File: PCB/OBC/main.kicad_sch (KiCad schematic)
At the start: 33 parts, among them J7 USB_C_Receptacle_USB2.0_16P, U2 STM32F405RGTx, U5 USBLC6-2SC6

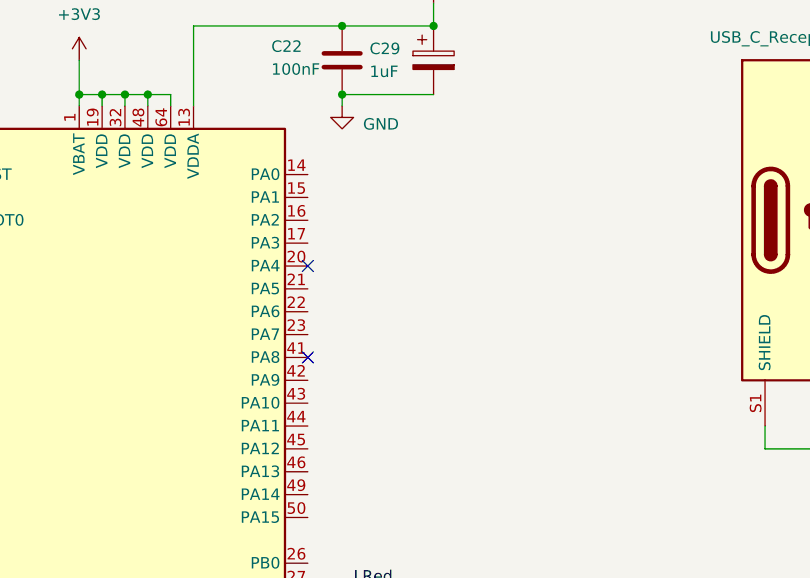
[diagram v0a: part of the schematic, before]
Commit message: Add: flash memory and mux at libraries
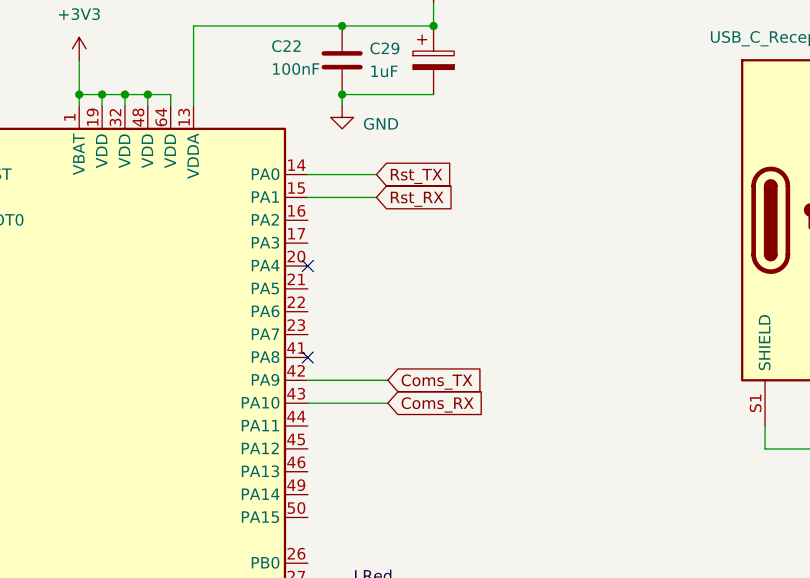
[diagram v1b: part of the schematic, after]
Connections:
- net Rst_TX: now reaches U2.14 (PA0)
- net Rst_RX: now reaches U2.15 (PA1)
- net Coms_TX: now reaches U2.42 (PA9)
- net Coms_RX: now reaches U2.43 (PA10)
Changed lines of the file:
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@@
+	(wire
+		(pts
+			(xy 156.21 67.31) (xy 165.1 67.31)
+		)
+		(stroke
+			(width 0)
+			(type default)
+		)
+	)
 	(wire
 		(pts
@@
 	(wire
 		(pts
+			(xy 156.21 46.99) (xy 163.83 46.99)
+		)
+		(stroke
+			(width 0)
+			(type default)
+		)
+	)
+	(wire
+		(pts
 			(xy 130.81 35.56) (xy 130.81 36.83)
 		)
@@
 	(wire
 		(pts
+			(xy 156.21 69.85) (xy 165.1 69.85)
+		)
+		(stroke
+			(width 0)
+			(type default)
+		)
+	)
+	(wire
+		(pts
 			(xy 73.66 26.67) (xy 62.23 26.67)
 		)
@@
 		(pts
 			(xy 233.68 41.91) (xy 229.87 41.91)
+		)
+		(stroke
+			(width 0)
+			(type default)
+		)
+	)
+	(wire
+		(pts
+			(xy 156.21 44.45) (xy 163.83 44.45)
 		)
 		(stroke
@@
 			)
 			(justify right bottom)
+		)
+	)
+	(global_label "Rst_RX"
+		(shape input)
+		(at 163.83 46.99 0)
+		(fields_autoplaced yes)
+		(effects
+			(font
+				(size 1.27 1.27)
+			)
+			(justify left)
+		)
+		(property "Intersheetrefs" "${INTERSHEET_REFS}"
+			(at 173.2861 46.99 0)
+			(effects
+				(font
+					(size 1.27 1.27)
+				)
+				(justify left)
+				(hide yes)
+			)
 		)
 	)
@@
 		)
 	)
+	(global_label "Coms_RX"
+		(shape input)
+		(at 165.1 69.85 0)
+		(fields_autoplaced yes)
+		(effects
+			(font
+				(size 1.27 1.27)
+			)
+			(justify left)
+		)
+		(property "Intersheetrefs" "${INTERSHEET_REFS}"
+			(at 176.6727 69.85 0)
+			(effects
+				(font
+					(size 1.27 1.27)
+				)
+				(justify left)
+				(hide yes)
+			)
+		)
+	)
 	(global_label "LDO_USB"
 		(shape input)
@@
 		)
 	)
+	(global_label "Coms_TX"
+		(shape input)
+		(at 165.1 67.31 0)
+		(fields_autoplaced yes)
+		(effects
+			(font
+				(size 1.27 1.27)
+			)
+			(justify left)
+		)
+		(property "Intersheetrefs" "${INTERSHEET_REFS}"
+			(at 176.3703 67.31 0)
+			(effects
+				(font
+					(size 1.27 1.27)
+				)
+				(justify left)
+				(hide yes)
+			)
+		)
+	)
 	(global_label "USB_D+"
 		(shape input)
@@
 			(effects
 				(font
+					(size 1.27 1.27)
+				)
+				(justify left)
+				(hide yes)
+			)
+		)
+	)
+	(global_label "Rst_TX"
+		(shape input)
+		(at 163.83 44.45 0)
+		(fields_autoplaced yes)
+		(effects
+			(font
+				(size 1.27 1.27)
+			)
+			(justify left)
+		)
+		(property "Intersheetrefs" "${INTERSHEET_REFS}"
+			(at 172.9837 44.45 0)
+			(effects
+				(font

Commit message: Watchdog
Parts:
- added C10, C11: 100nF, symbol Device:C
- added C12: 1uF, symbol Device:C
- added R3, R4: 10k, symbol Device:R
- added U3: W25Q128JVSIQ, SOIC_128JVSIQ_WIN, symbol W25Q128JVSIQ:W25Q128JVSIQ
- added U6: TMUX1574PWR, PWP16_2P31X2P46_TEX, symbol TMUX1574PWR:TMUX1574PWR
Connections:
- net +3V3: now also C10.1, C11.1, C12.1, R3.2, R4.1, U3.8 (VCC), U6.16 (VDD)
- net GND: now also C10.2, C11.2, C12.2, U3.1 (/CS), U3.4 (GND), U6.15 (*EN), U6.8 (GND)
- new net: R3.1, U3.3
- new net: R4.2, U3.7 (/HOLD_or_/RESET_(IO3))
- new net py_flash_clk_m: U3.6 (CLK), U6.12 (D4)
- new net py_flash_miso_m: U3.2 (DO_(IO1)), U6.7 (D2)
- new net py_flash_mosi_m: U3.5 (DI_(IO0)), U6.9 (D3)
- new net select_py: U6.1 (SEL)
- no-connect marks 9 -> 10
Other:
- moved on the sheet: C20, C21, C22, C29, C32, D3, D7, D8, J7, R14, R15, R16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

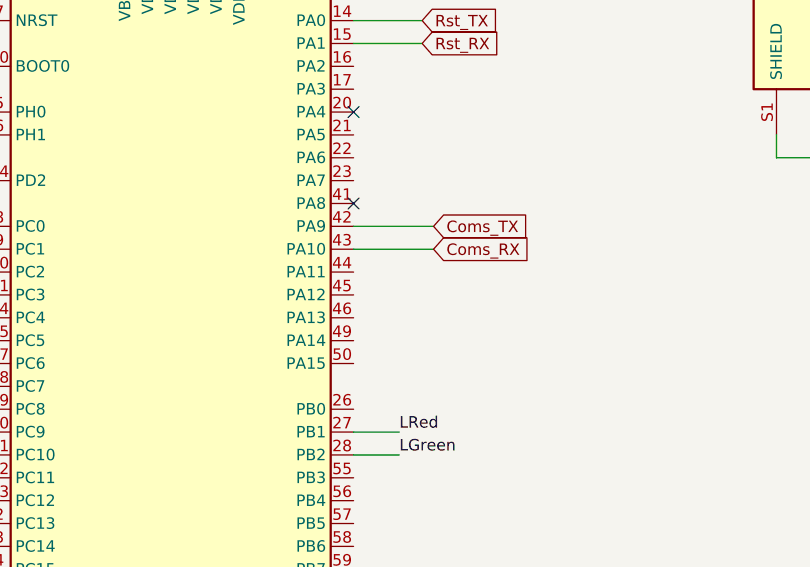
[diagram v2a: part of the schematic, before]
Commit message: Colocacion de OCP, LDO
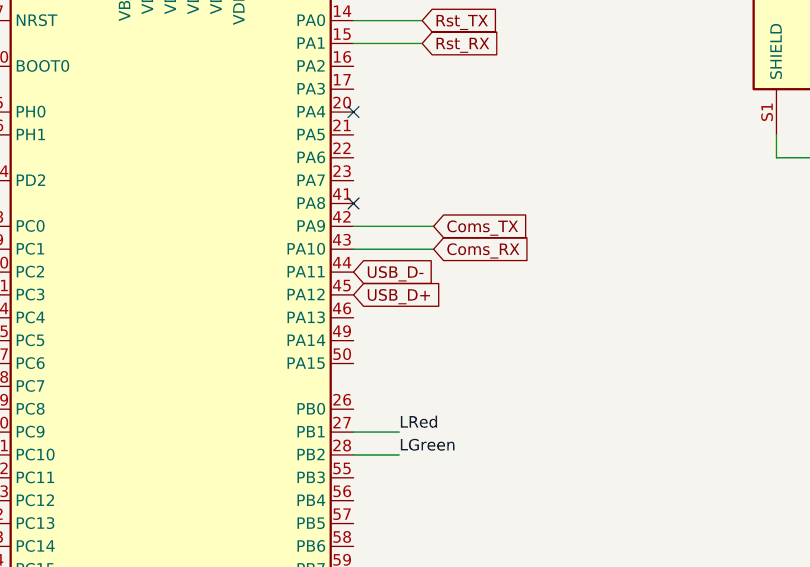
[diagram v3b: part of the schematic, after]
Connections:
- net USB_D+: now also U2.45 (PA12)
- net USB_D-: now also U2.44 (PA11)
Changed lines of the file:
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@@
+	(global_label "USB_D-"
+		(shape input)
+		(at 143.51 77.47 0)
+		(fields_autoplaced yes)
+		(effects
+			(font
+				(size 1.27 1.27)
+			)
+			(justify left)
+		)
+		(property "Intersheetrefs" "${INTERSHEET_REFS}"
+			(at 154.1152 77.47 0)
+			(effects
+				(font
+					(size 1.27 1.27)
+				)
+				(justify left)
+				(hide yes)
+			)
+		)
+	)
 	(global_label "USB_D-"
 		(shape input)
@@
 			(effects
 				(font
+					(size 1.27 1.27)
+				)
+				(justify left)
+				(hide yes)
+			)
+		)
+	)
+	(global_label "USB_D+"
+		(shape input)
+		(at 143.51 80.01 0)
+		(fields_autoplaced yes)
+		(effects
+			(font
+				(size 1.27 1.27)
+			)
+			(justify left)
+		)
+		(property "Intersheetrefs" "${INTERSHEET_REFS}"
+			(at 154.1152 80.01 0)
+			(effects
+				(font

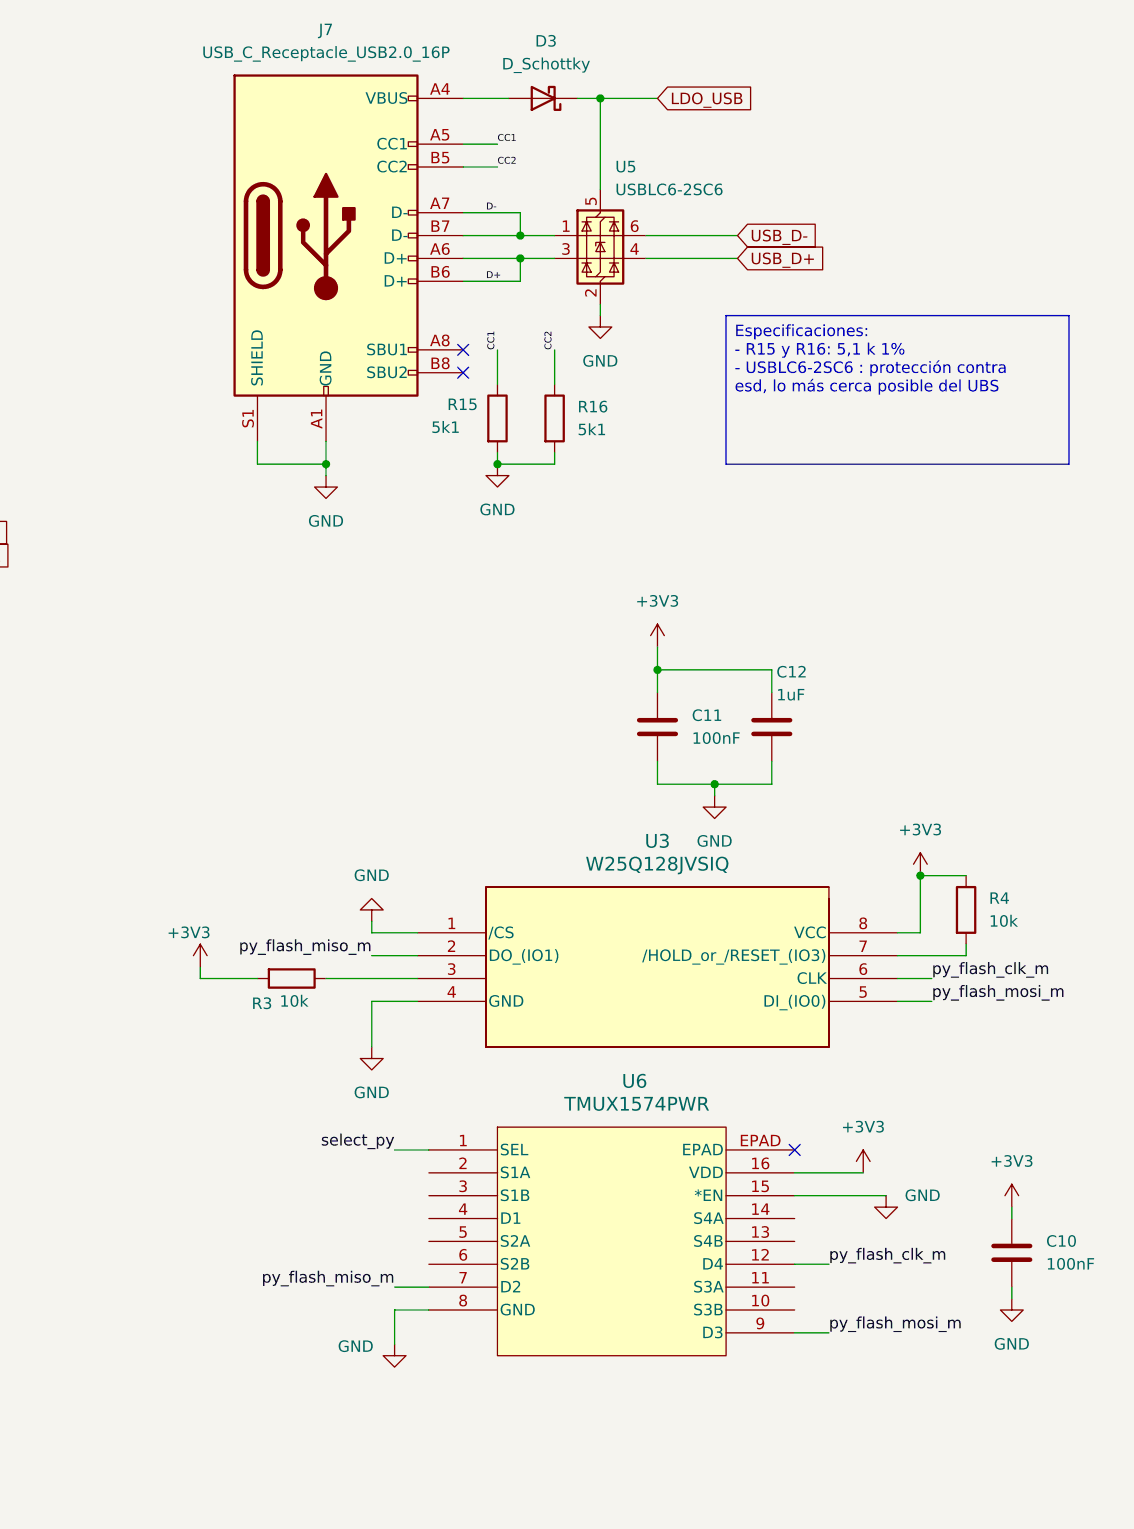
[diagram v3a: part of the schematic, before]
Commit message: Add: Can bus
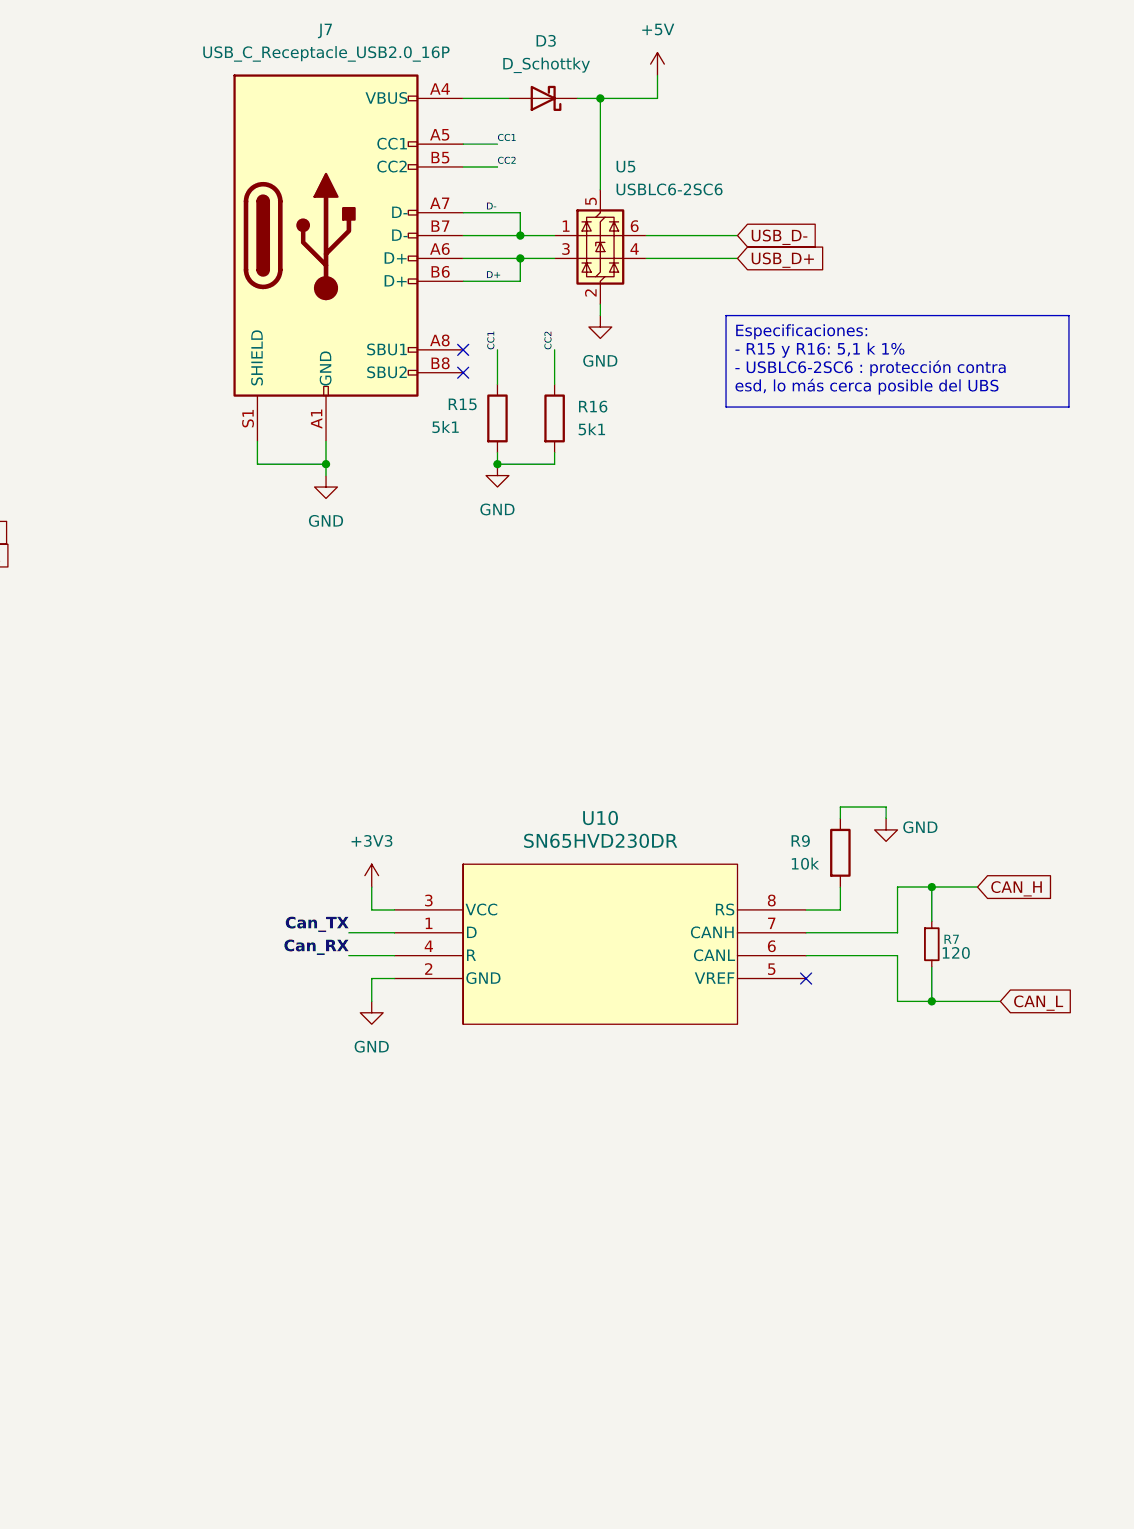
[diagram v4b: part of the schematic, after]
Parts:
- removed C10, C11: 100nF, symbol Device:C
- removed C12: 1uF, symbol Device:C
- removed R3, R4: 10k, symbol Device:R
- removed U3: W25Q128JVSIQ, SOIC_128JVSIQ_WIN, symbol W25Q128JVSIQ:W25Q128JVSIQ
- removed U6: TMUX1574PWR, PWP16_2P31X2P46_TEX, symbol TMUX1574PWR:TMUX1574PWR
- added R7: 120, symbol Device:R_Small
- added R9: 10k, symbol Device:R
- added U10: SN65HVD230DR, D8, symbol SN65HVD230DR:SN65HVD230DR
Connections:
- net +3V3: now also U10.3 (VCC)
- net GND: now also R9.1, U10.2 (GND)
- net LDO_USB renamed +5V
- new net: R9.2, U10.8 (RS)
- new net CAN_H: R7.1, U10.7 (CANH)
- new net CAN_L: R7.2, U10.6 (CANL)
- new net Can_RX: U10.4 (R)
- new net Can_TX: U10.1 (D)

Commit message: minors changes
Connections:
- net SWDIO1: now reaches U2.46 (PA13)
- net SWCLK1: now reaches U2.49 (PA14)
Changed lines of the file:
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@@
 	(wire
 		(pts
-			(xy 143.51 72.39) (xy 152.4 72.39)
+			(xy 143.51 72.39) (xy 151.13 72.39)
 		)
 		(stroke
@@
 	(wire
 		(pts
+			(xy 143.51 85.09) (xy 151.13 85.09)
+		)
+		(stroke
+			(width 0)
+			(type default)
+		)
+	)
+	(wire
+		(pts
+			(xy 151.13 80.01) (xy 143.51 80.01)
+		)
+		(stroke
+			(width 0)
+			(type default)
+		)
+	)
+	(wire
+		(pts
 			(xy 39.37 35.56) (xy 27.94 35.56)
 		)
@@
 	(wire
 		(pts
+			(xy 151.13 77.47) (xy 143.51 77.47)
+		)
+		(stroke
+			(width 0)
+			(type default)
+		)
+	)
+	(wire
+		(pts
 			(xy 63.5 46.99) (xy 63.5 49.53)
 		)
@@
 	(wire
 		(pts
+			(xy 143.51 82.55) (xy 151.13 82.55)
+		)
+		(stroke
+			(width 0)
+			(type default)
+		)
+	)
+	(wire
+		(pts
 			(xy 265.43 120.65) (xy 265.43 124.46)
 		)
@@
 	(wire
 		(pts
-			(xy 143.51 74.93) (xy 152.4 74.93)
+			(xy 143.51 74.93) (xy 151.13 74.93)
 		)
 		(stroke
@@
 	(global_label "USB_D-"
 		(shape input)
-		(at 143.51 77.47 0)
+		(at 151.13 77.47 0)
 		(fields_autoplaced yes)
 		(effects
@@
 		)
 		(property "Intersheetrefs" "${INTERSHEET_REFS}"
-			(at 154.1152 77.47 0)
+			(at 161.7352 77.47 0)
 			(effects
 				(font
@@
 	(global_label "Coms_RX"
 		(shape input)
-		(at 152.4 74.93 0)
+		(at 151.13 74.93 0)
 		(fields_autoplaced yes)
 		(effects
@@
 		)
 		(property "Intersheetrefs" "${INTERSHEET_REFS}"
-			(at 163.9727 74.93 0)
+			(at 162.7027 74.93 0)
+			(effects
+				(font
+					(size 1.27 1.27)
+				)
+				(justify left)
+				(hide yes)
+			)
+		)
+	)
+	(global_label "SWDIO1"
+		(shape input)
+		(at 151.13 82.55 0)
+		(fields_autoplaced yes)
+		(effects
+			(font
+				(size 1.27 1.27)
+			)
+			(justify left)
+		)
+		(property "Intersheetrefs" "${INTERSHEET_REFS}"
+			(at 161.1909 82.55 0)
+			(effects
+				(font
+					(size 1.27 1.27)
+				)
+				(justify left)
+				(hide yes)
+			)
+		)
+	)
+	(global_label "SWCLK1"
+		(shape input)
+		(at 151.13 85.09 0)
+		(fields_autoplaced yes)
+		(effects
+			(font
+				(size 1.27 1.27)
+			)
+			(justify left)
+		)
+		(property "Intersheetrefs" "${INTERSHEET_REFS}"
+			(at 161.5537 85.09 0)
 			(effects
 				(font
@@
 	(global_label "Coms_TX"
 		(shape input)
-		(at 152.4 72.39 0)
+		(at 151.13 72.39 0)
 		(fields_autoplaced yes)
 		(effects
@@
 		)
 		(property "Intersheetrefs" "${INTERSHEET_REFS}"
-			(at 163.6703 72.39 0)
+			(at 162.4003 72.39 0)
 			(effects
 				(font
@@
 	(global_label "USB_D+"
 		(shape input)
-		(at 143.51 80.01 0)
+		(at 151.13 80.01 0)
 		(fields_autoplaced yes)
 		(effects
@@
 		)
 		(property "Intersheetrefs" "${INTERSHEET_REFS}"
-			(at 154.1152 80.01 0)
+			(at 161.7352 80.01 0)
 			(effects
 				(font

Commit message: cambiode OCP
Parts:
- removed C20, C21: 2.2uF, Capacitor_SMD:C_0805_2012Metric_Pad1.18x1.45mm_HandSolder, symbol Device:C
- removed C24, C26: 100nF, Capacitor_SMD:C_0805_2012Metric_Pad1.18x1.45mm_HandSolder, symbol Device:C
- removed C25, C32: 100nF, Capacitor_SMD:C_0603_1608Metric_Pad1.08x0.95mm_HandSolder, symbol Device:C
- removed C28: 4.7u, Capacitor_SMD:C_0805_2012Metric_Pad1.18x1.45mm_HandSolder, symbol Device:C_Polarized
- removed C29: 1uF, Capacitor_SMD:C_0805_2012Metric_Pad1.18x1.45mm_HandSolder, symbol Device:C_Polarized
- removed C5: 15pF, Capacitor_SMD:C_0603_1608Metric_Pad1.08x0.95mm_HandSolder, symbol Device:C
- removed D8: LED, LED_SMD:LED_0805_2012Metric_Pad1.15x1.40mm_HandSolder, symbol Device:LED
- removed U2: STM32F405RGTx, Package_QFP:LQFP-64_10x10mm_P0.5mm, symbol MCU_ST_STM32F4:STM32F405RGTx
- added C1: 4.7u, Capacitor_SMD:C_0805_2012Metric_Pad1.18x1.45mm_HandSolder, symbol Device:C_Polarized
- added C10, C2: 15pF, Capacitor_SMD:C_0603_1608Metric_Pad1.08x0.95mm_HandSolder, symbol Device:C
- added C11: 100nF, Capacitor_SMD:C_0805_2012Metric_Pad1.18x1.45mm_HandSolder, symbol Device:C
- added C12, C15: 2.2uF, Capacitor_SMD:C_0805_2012Metric_Pad1.18x1.45mm_HandSolder, symbol Device:C
- added C14, C9: 100nF, Capacitor_SMD:C_0603_1608Metric_Pad1.08x0.95mm_HandSolder, symbol Device:C
- added C17: 1uF, Capacitor_SMD:C_0805_2012Metric_Pad1.18x1.45mm_HandSolder, symbol Device:C_Polarized
- added D1: LED, LED_SMD:LED_0805_2012Metric_Pad1.15x1.40mm_HandSolder, symbol Device:LED
- added U1: STM32F405RGTx, Package_QFP:LQFP-64_10x10mm_P0.5mm, symbol MCU_ST_STM32F4:STM32F405RGTx
- C6: value 15pF -> 100nF; footprint Capacitor_SMD:C_0603_1608Metric_Pad1.08x0.95mm_HandSolder -> Capacitor_SMD:C_0805_2012Metric_Pad1.18x1.45mm_HandSolder; LCSC Part Name C1644 -> C1711
- LSE1: footprint ndx32khz:XTAL_NX3215SA_NDK -> XTAL_NX3215SA_NDK:XTAL_NX3215SA_NDK
- U2: renamed from U10; footprint D8 -> SN65HVD230DR:D8
- XTAL1: footprint ESCMHZ:ECS-80-12_ECS -> ECS-80-12-30BQ-JES-TR:ECS-80-12_ECS
- renumbered C23 to C13, C22 to C16, C30 to C3, C27 to C4, C7 to C5, C31 to C7, D7 to D2, J7 to J3, R14 to R1, R19 to R2, R20 to R3, R15 to R4, R16 to R5, R9 to R6, U5 to U3
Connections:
- net +3V3: now also C6.1, C1.1, C11.1, C9.1, U1.1 (VBAT), U1.19 (VDD), U1.32 (VDD), U1.48 (VDD), U1.64 (VDD)
- net +3V3A: now also C17.1, U1.13 (VDDA)
- net BOOT0: now also U1.60 (BOOT0)
- net Coms_RX: now also U1.43 (PA10)
- net Coms_TX: now also U1.42 (PA9)
- net GND: now also C1.2, C10.2, C11.2, C12.2, C14.2, C15.2, C17.2, C2.2, C9.2, D1.1 (K), U1.12 (VSSA), U1.18 (VSS), U1.63 (VSS)
- net HSE_IN: now also C2.1, U1.5 (PH0); no longer C6.1
- net HSE_OUT: now also C10.1, U1.6 (PH1)
- net LGreen: now also U1.28 (PB2)
- net LRed: now also U1.27 (PB1)
- net LSE_IN: now also U1.3 (PC14)
- net LSE_OUT: now also U1.4 (PC15)
- net Rst_RX: now also U1.15 (PA1)
- net Rst_TX: now also U1.14 (PA0)
- net SWCLK1: now also U1.49 (PA14)
- net SWDIO1: now also U1.46 (PA13)
- net SWD_NRST: now also C14.1, U1.7 (NRST)
- net USB_D+: now also U1.45 (PA12)
- net USB_D-: now also U1.44 (PA11)
- net at R2.2: now also D1.2 (A)
- new net: C15.1, U1.47 (VCAP_2)
- new net: C12.1, U1.31 (VCAP_1)
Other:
- moved on the sheet: R6, R7, U2

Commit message: Cambio de OCP
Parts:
- U2: LCSC Part Name (none) -> C12084

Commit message: BoomColumnaAmarilla
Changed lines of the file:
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@@
+		)
+	)
+	(global_label "5V"
+		(shape input)
+		(at 228.6 24.13 90)
+		(fields_autoplaced yes)
+		(effects
+			(font
+				(size 1.27 1.27)
+			)
+			(justify left)
+		)
+		(property "Intersheetrefs" "${INTERSHEET_REFS}"
+			(at 228.6 18.8467 90)
+			(effects
+				(font
+					(size 1.27 1.27)
+				)
+				(justify left)
+				(hide yes)
+			)
 		)
 	)
